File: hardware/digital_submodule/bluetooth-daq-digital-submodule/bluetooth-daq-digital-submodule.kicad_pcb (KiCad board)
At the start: 2 copper layers, 145.3 x 150.9 mm, 142 parts, among them J1 MCU I/F, J2 Digital Inputs, J3 Digital Outputs, J4 Communication I/F, J5 RS-485 I/F, U1 74HC595, U2 74HC595, U3 74HC165, U4 74HC165, U5 24LC1025, U6 SN75176AD, U7 CD4053B, U8 CD4053B

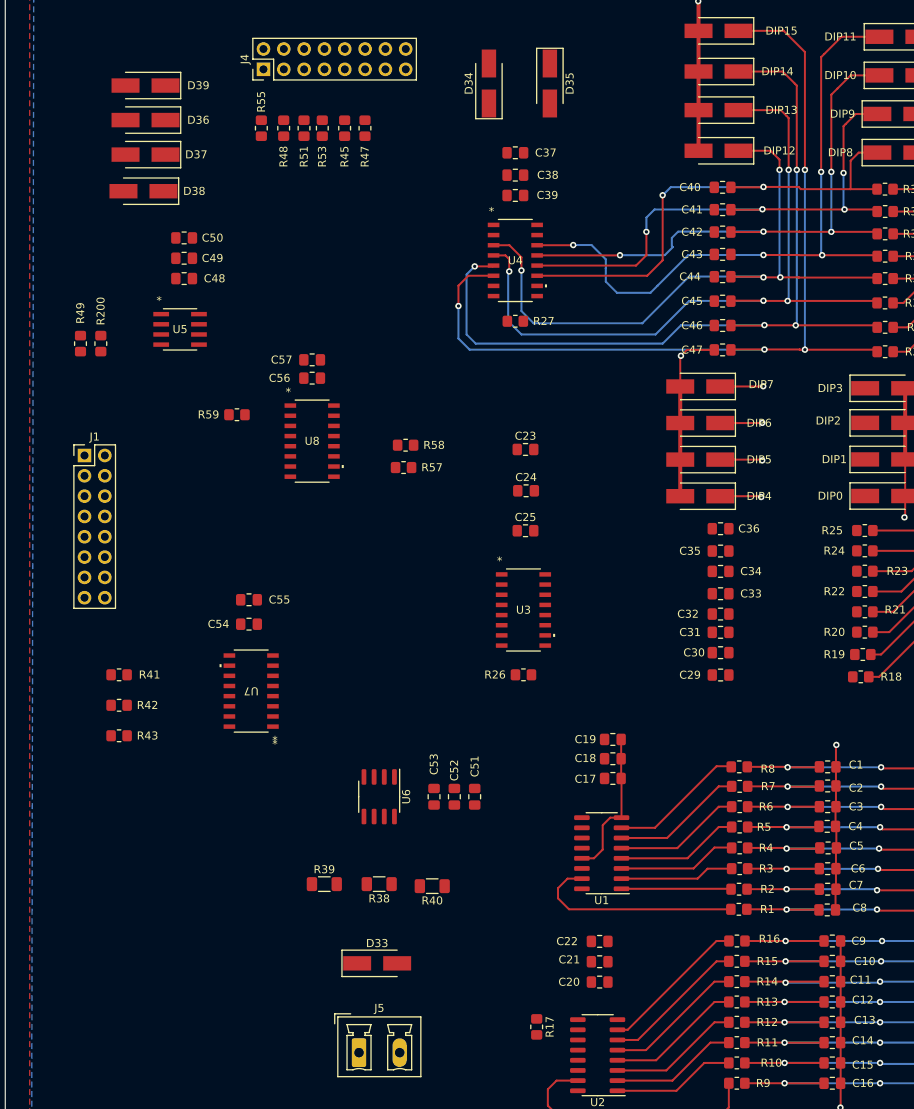
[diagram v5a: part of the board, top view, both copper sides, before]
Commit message: Performed routing for interface section for digital submodule.
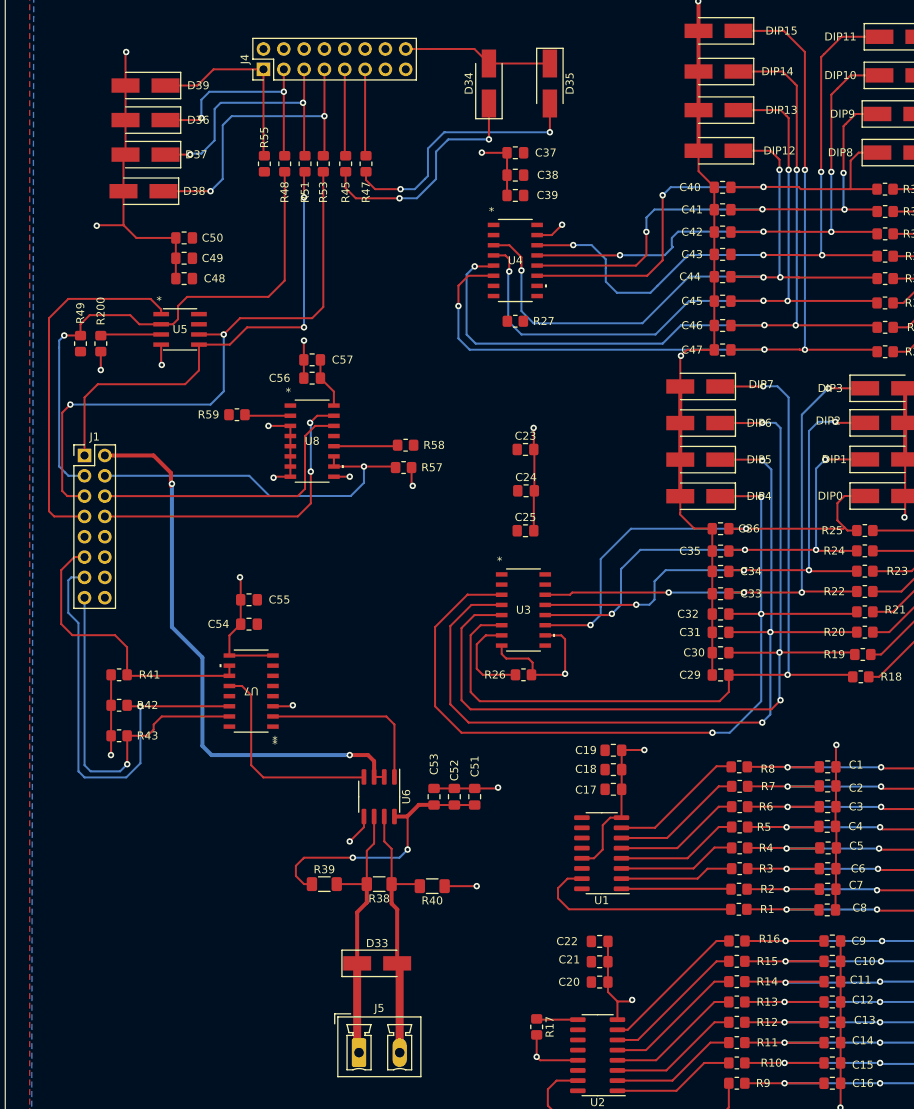
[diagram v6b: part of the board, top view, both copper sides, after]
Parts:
- moved R55 4.46 mm to (118.5, 97.9)
- moved R45 4.45 mm to (128.7, 97.9)
- moved R47 4.45 mm to (131.2, 97.9)
- moved R48 4.45 mm to (121.0, 97.9)
- moved R51 4.45 mm to (123.6, 97.9)
- moved R53 4.45 mm to (125.9, 97.9)
- moved C18 1.36 mm to (162.1, 173.6)
- moved C17 1.36 mm to (162.1, 176.1)
- moved C19 1.36 mm to (162.1, 171.2)
- turned C57 to 180 degrees
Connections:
- J1 pad 11: XSPI_SEL -> UART_SEL
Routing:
- net GND: track 136.2 -> 378.1 mm, vias 6 -> 28
- net Net-(R19-Pad2): track 5.44 -> 113.3 mm, vias 1 -> 3
- net Net-(R20-Pad2): track 5.29 -> 112.2 mm, vias 1 -> 3
- net Net-(U3-Pad3): track 5.52 -> 110.5 mm, vias 1 -> 3
- net Net-(R18-Pad2): track 5.74 -> 106.3 mm, vias 1 -> 2
- net SCLK: track 0.00 -> 75.1 mm, vias 0 -> 2
- net Net-(R22-Pad2): track 0.00 -> 72.6 mm, vias 0 -> 4
- net XCVR_DRV_EN: track 0.00 -> 70.9 mm, vias 0 -> 2
- net Net-(R23-Pad2): track 0.18 -> 69.2 mm, vias 0 -> 4
- net MISO: track 0.00 -> 67.1 mm, vias 0 -> 1
- net Net-(U3-Pad12): track 0.00 -> 63.8 mm, vias 0 -> 4
- net MOSI: track 0.00 -> 59.7 mm, vias 0 -> 2
- net Net-(U3-Pad11): track 0.00 -> 57.7 mm, vias 0 -> 2
- net UART_TX: track 0.00 -> 55.3 mm, vias 0 -> 1
- net I2C_SEL: track 0.00 -> 45.2 mm, vias 0 -> 1
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
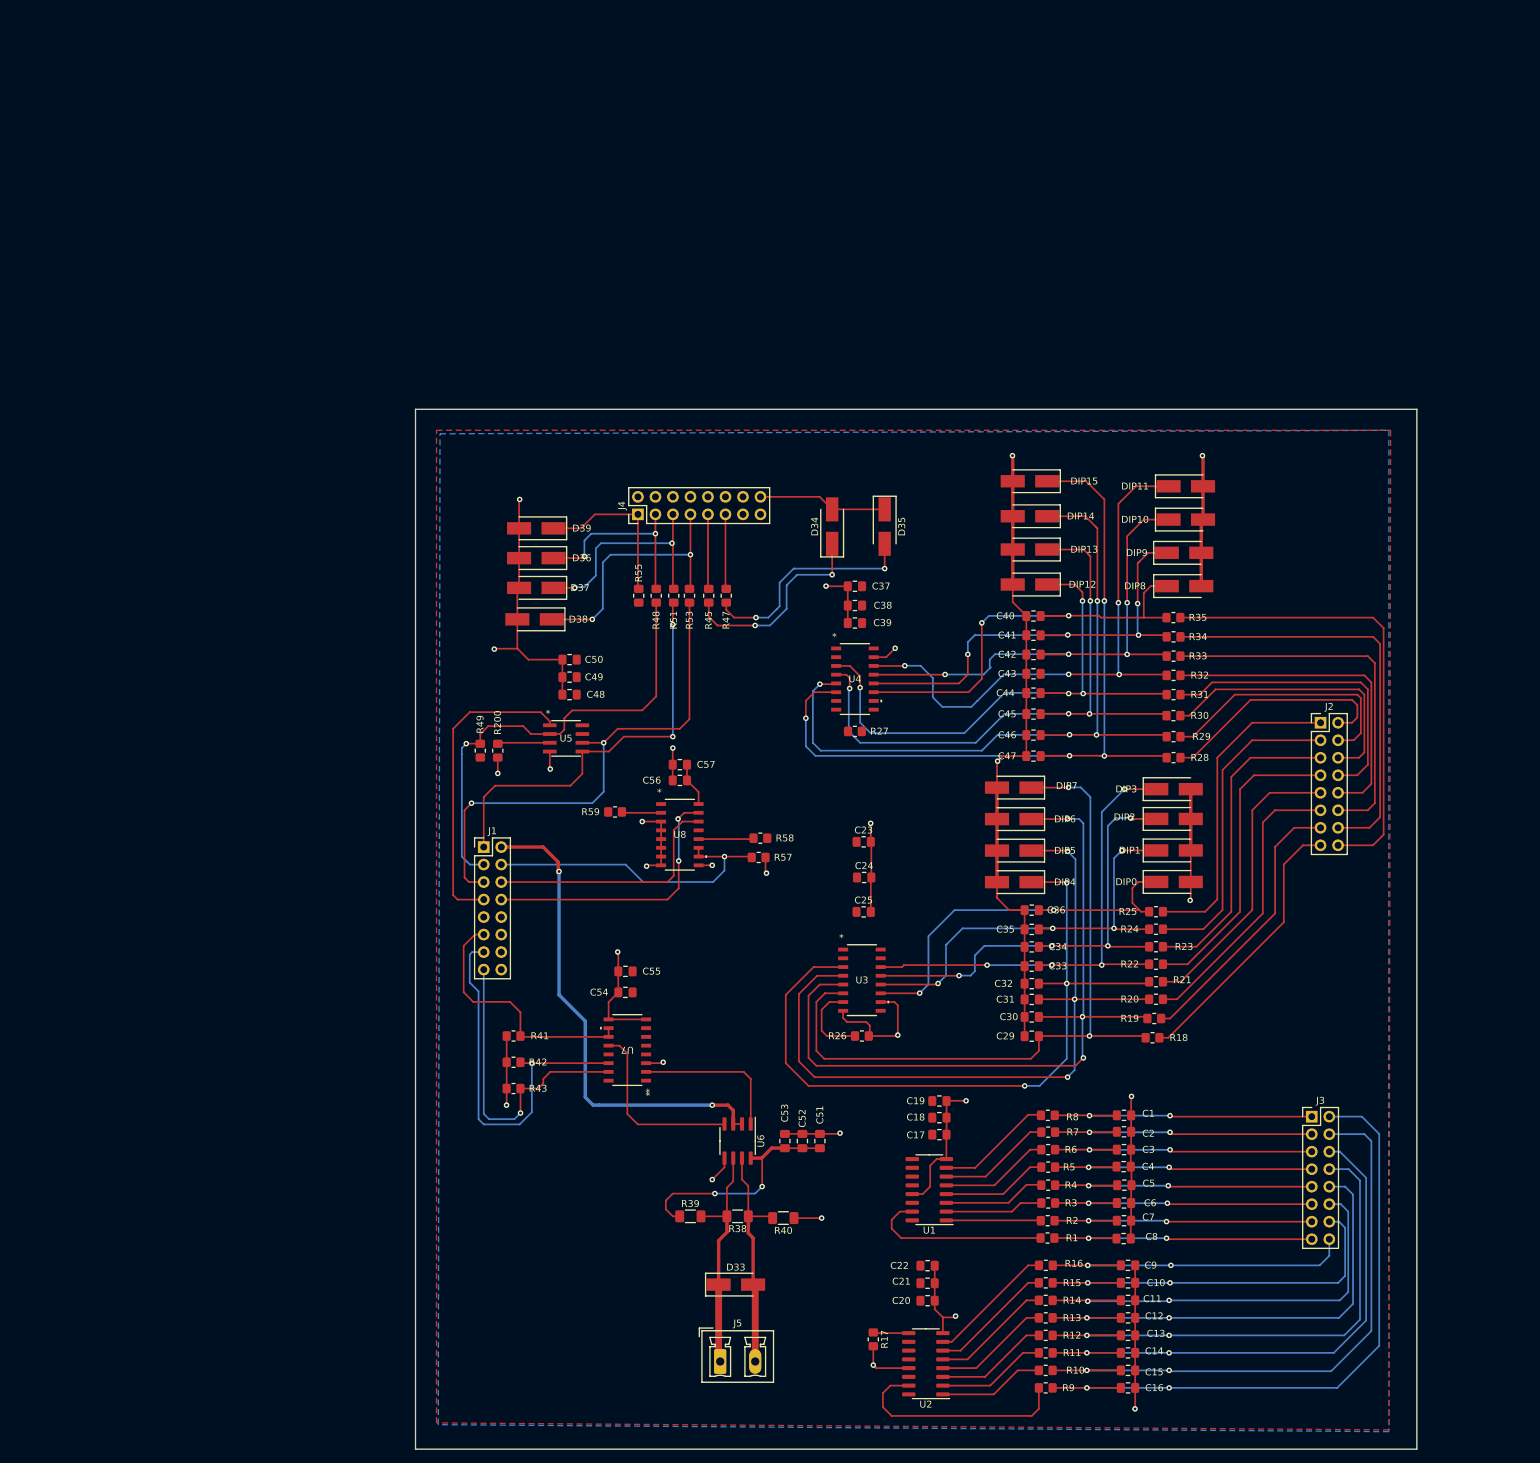
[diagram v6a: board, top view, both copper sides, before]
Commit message: Completed initial routing of digital sub module
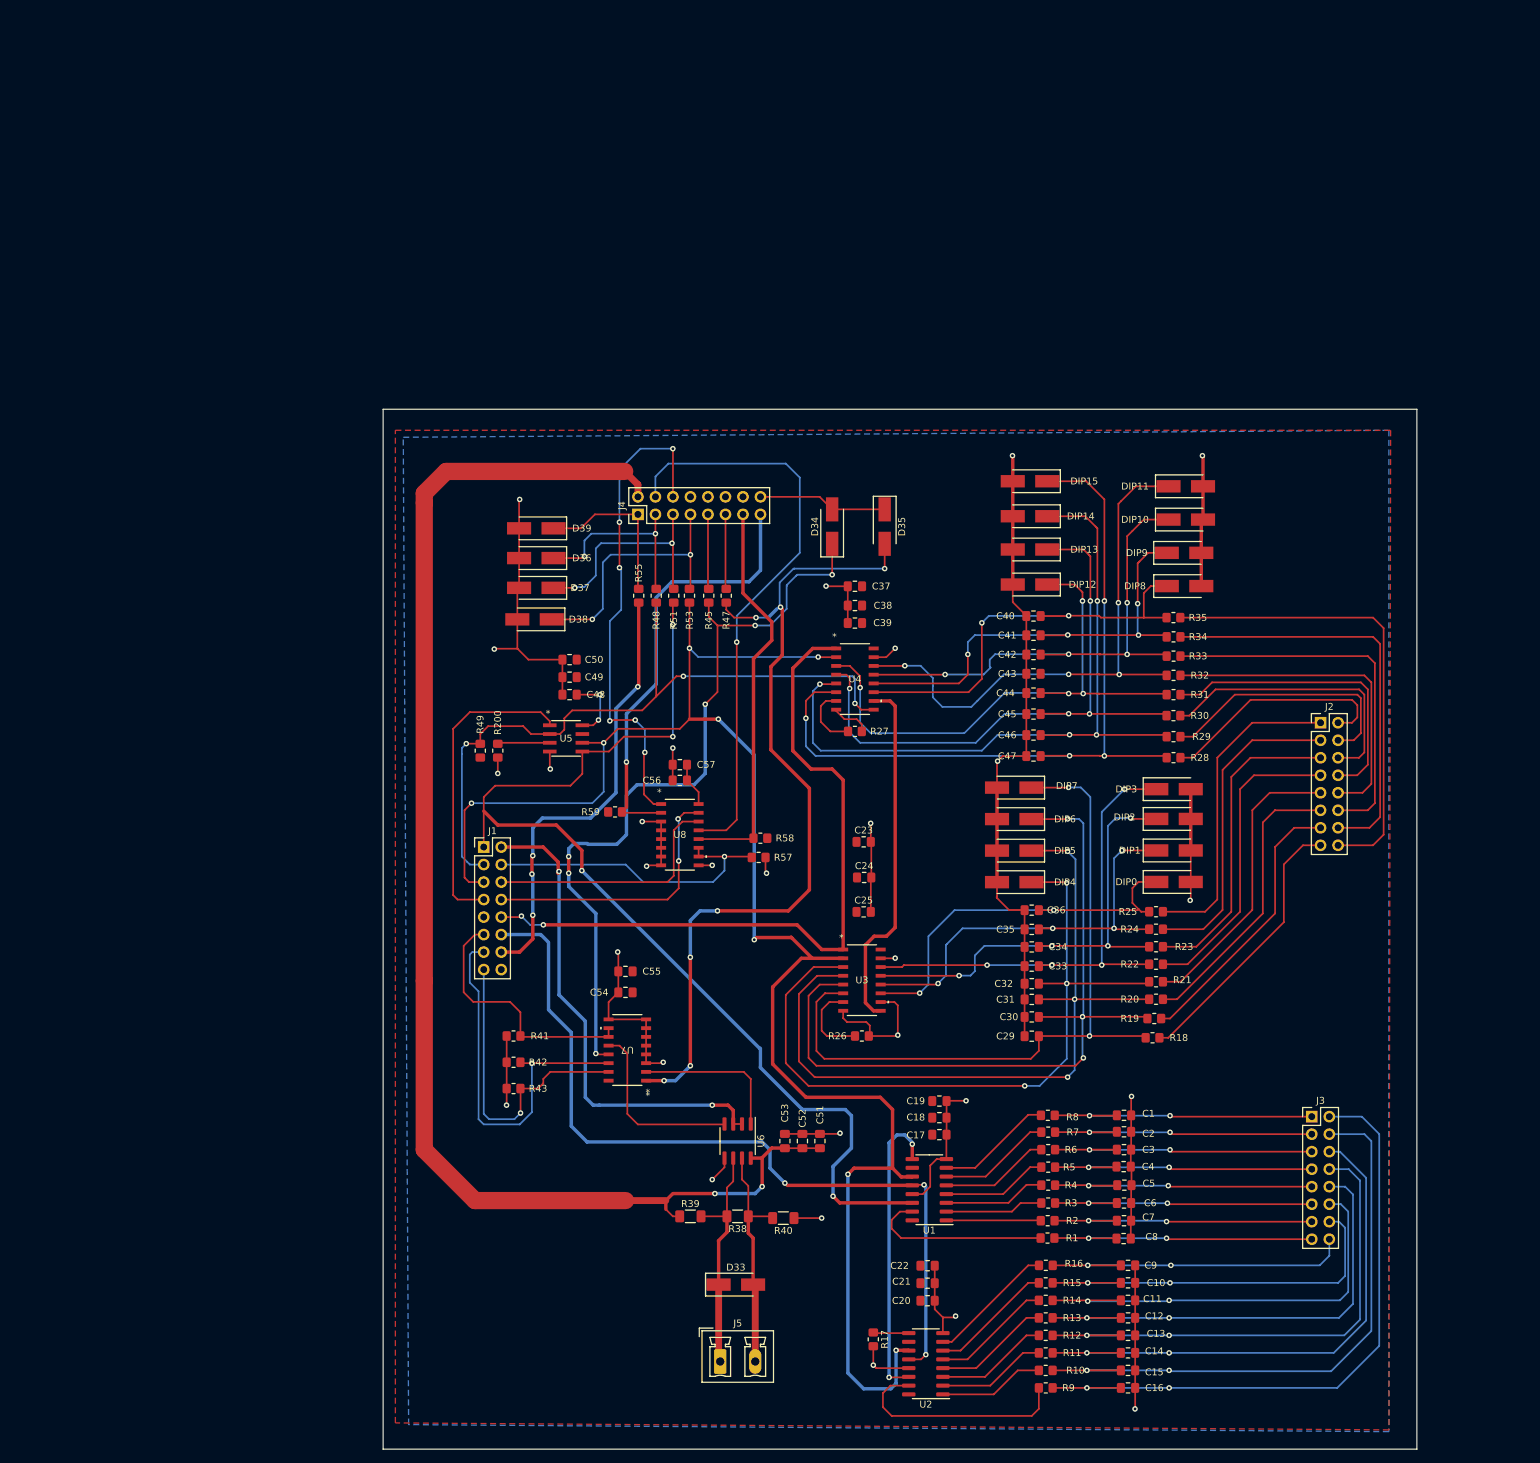
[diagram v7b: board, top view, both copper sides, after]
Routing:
- net SCLK: track 75.1 -> 251.0 mm, vias 2 -> 8
- net 5V: track 33.3 -> 201.5 mm
- net DO_LOAD: track 0.00 -> 119.2 mm, vias 0 -> 3
- net DI_LOAD: track 0.00 -> 104.8 mm, vias 0 -> 2
- net MOSI: track 59.7 -> 159.5 mm, vias 2 -> 4
- net Net-(D35-Pad2): track 33.0 -> 124.9 mm, vias 2 -> 7
- net I2C_SDA_OUT: track 0.00 -> 85.1 mm, vias 0 -> 1
- net Net-(D34-Pad1): track 30.0 -> 113.3 mm, vias 2 -> 6
- net I2C_SCL_OUT: track 0.00 -> 71.5 mm, vias 0 -> 6
- net XSPI_SEL: track 0.00 -> 64.7 mm, vias 0 -> 4
- net XI2C_SCL: track 5.73 -> 63.8 mm, vias 0 -> 1
- net Net-(U3-Pad9): track 0.00 -> 52.0 mm
- net XI2C_SDA: track 8.02 -> 57.8 mm
- net Net-(U1-Pad9): track 0.00 -> 43.9 mm, vias 0 -> 2
- net MISO: track 67.1 -> 103.9 mm, vias 1 -> 3
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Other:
- board size 145.3 x 150.9 mm -> 150 x 150.9 mm

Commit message: Performed first successful initial PCB routing
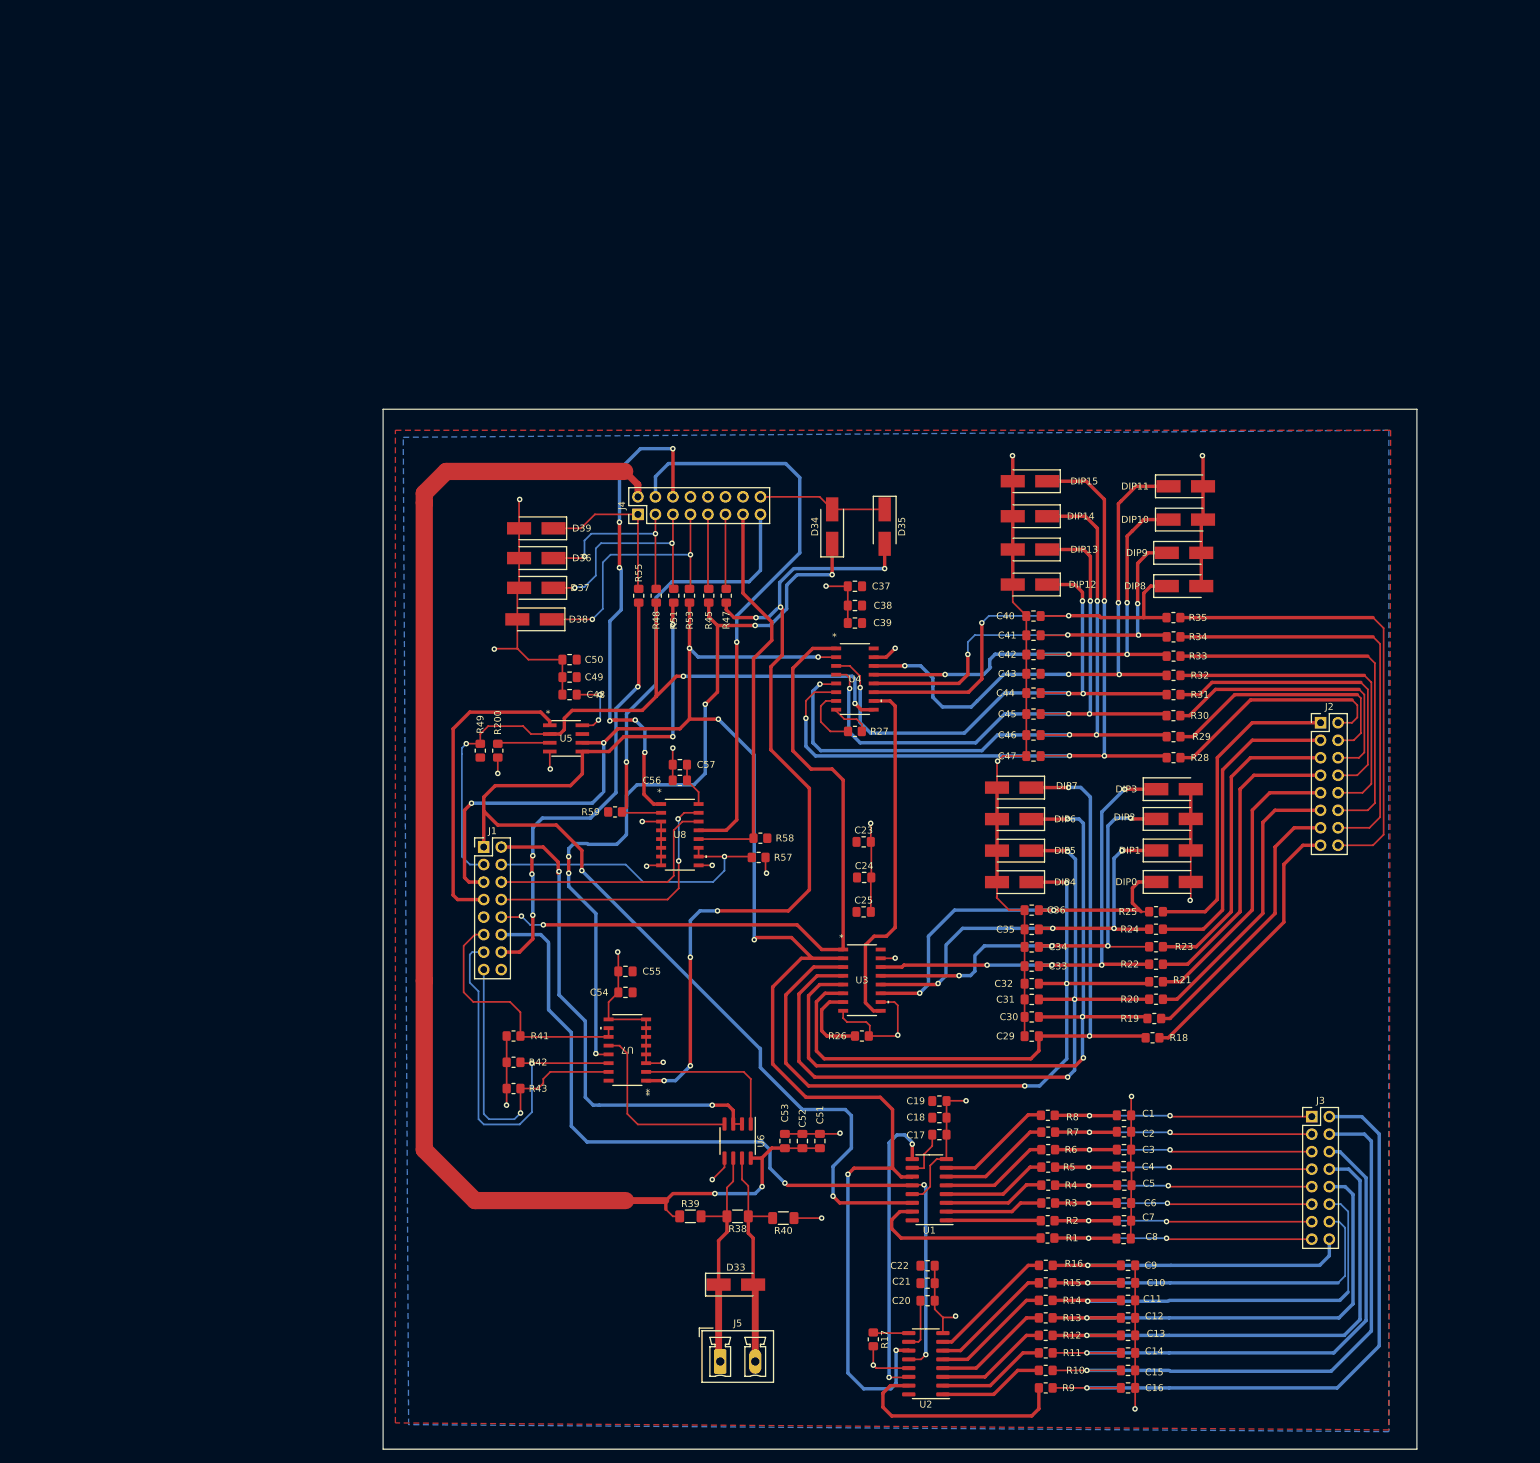
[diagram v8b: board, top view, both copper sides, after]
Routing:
- net 3V3: track 16.3 -> 30.9 mm
- net DOUT9: vias 2 -> 1
- net DOUT8: vias 2 -> 1
- net DOUT15: vias 2 -> 1
- net DOUT14: vias 2 -> 1
- net DOUT13: vias 2 -> 1
- net DOUT12: vias 2 -> 1
- net DOUT11: vias 2 -> 1
- net DOUT10: vias 2 -> 1
